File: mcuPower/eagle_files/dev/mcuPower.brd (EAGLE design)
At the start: 30 x 51 mm, 8 parts, among them P1 CR2032, P2 CR2032, U1 PQ070XF01SZH

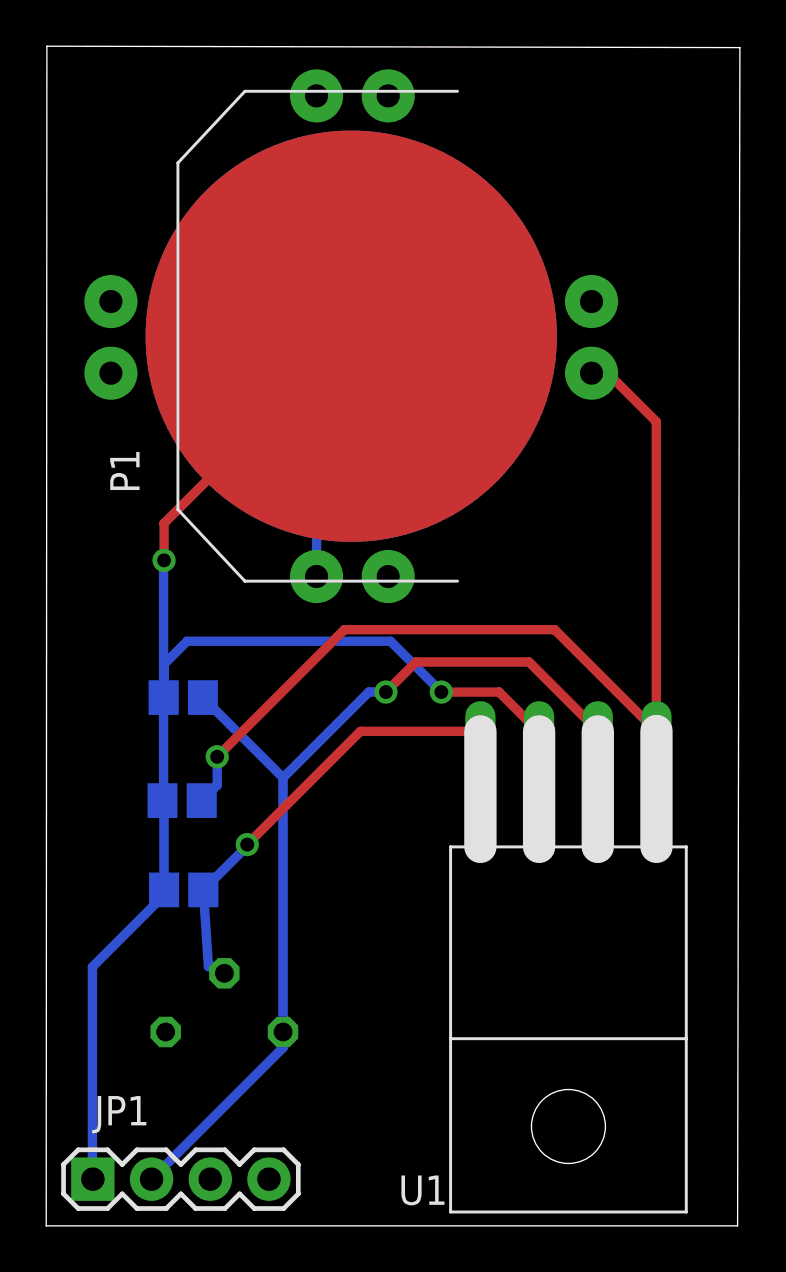
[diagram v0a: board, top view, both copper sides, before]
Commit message: new consolidated mcuPower.brd
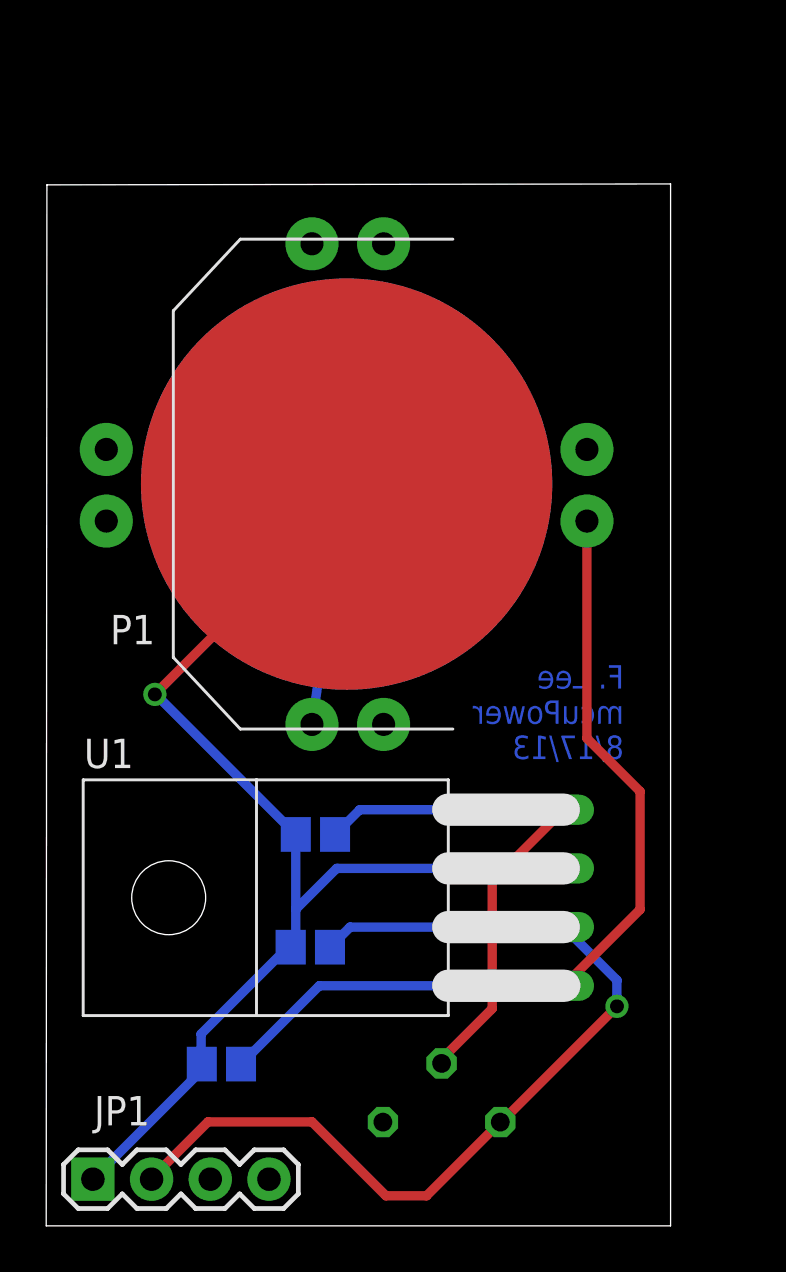
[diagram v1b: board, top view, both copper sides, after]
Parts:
- moved U1 14.8 mm to (9.10, 14.2), turned to 90 degrees
- moved C2 12.1 mm to (11.4, 12.1)
- moved C1 11.5 mm to (7.58, 7.00)
- moved R2 10.2 mm to (17.1, 4.49)
- moved P1 6.40 mm to (13.0, 32.1)
- moved P2 6.40 mm to (13.0, 32.1)
- moved R1 6.18 mm to (11.7, 16.9)
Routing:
- net GND: track 60.9 -> 52.1 mm, vias 2 -> 1
- net VCC: track 42.3 -> 37.8 mm, vias 1 -> 0
- net N$2: track 19.2 -> 23.5 mm, vias 1 -> 0
- net VOUT: track 41.6 -> 40.8 mm
- net N$1: track 11.0 -> 10.5 mm
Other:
- board size 30 x 51 mm -> 27 x 45.1 mm
- board text added: "F. Lee mcuPower 8/17/13"
